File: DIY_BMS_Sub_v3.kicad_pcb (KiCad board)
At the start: 4 copper layers, 70 x 70 mm, 112 parts, among them J1 Conn_01x11, J2 Conn_02x04_Top_Bottom, J3 Conn_02x03_Top_Bottom, J4 Conn_02x03_Top_Bottom, Q1 Q_NMOS_GSD, Q2 Q_NMOS_GSD, Q3 Q_NMOS_GSD, Q4 Q_NMOS_GSD, Q5 Q_NMOS_GSD, Q6 Q_NMOS_GSD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

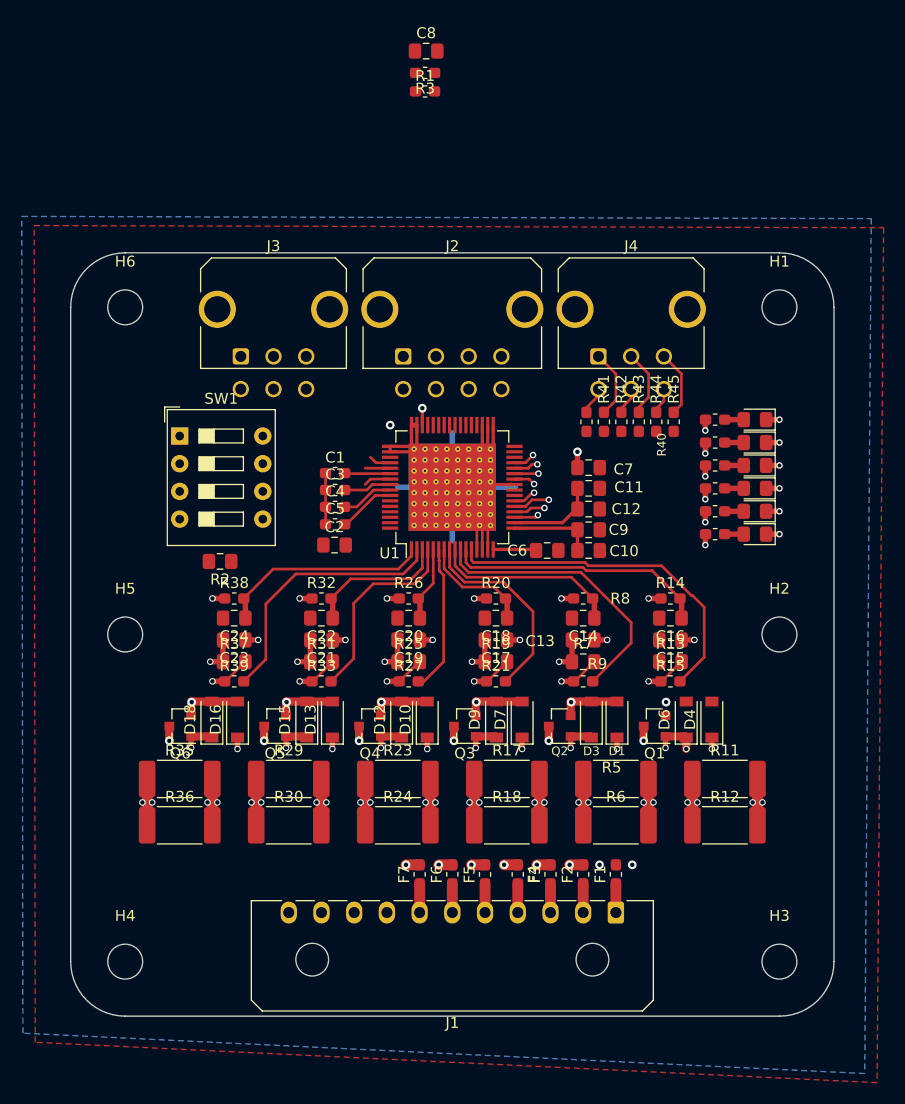
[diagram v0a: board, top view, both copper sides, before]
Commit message: Add files via upload
Routed the PCB further (switch-, NORTH- and thermistor still have to be done). Made silkscreen spacing more consistant overall. Added 3d-files for Molex-connectors.
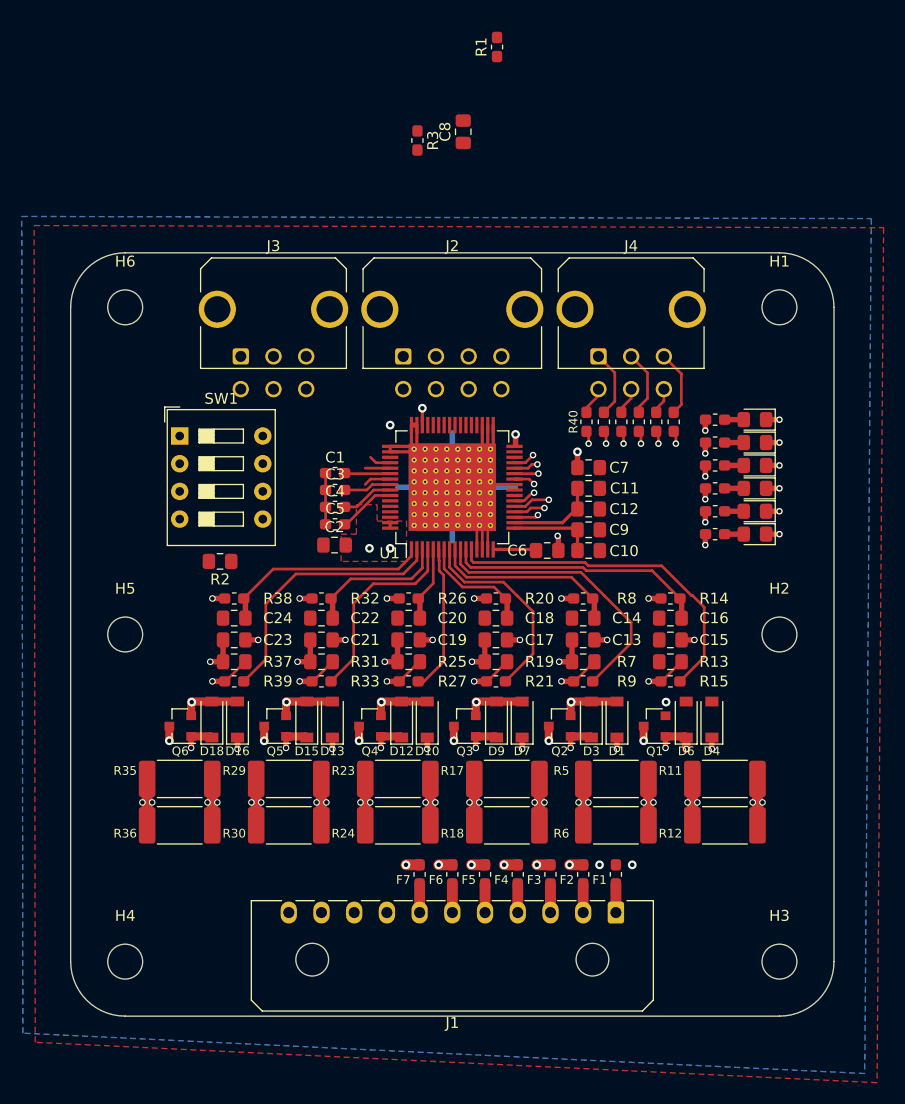
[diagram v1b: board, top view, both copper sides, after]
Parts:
- moved C8 8.14 mm to (1.00, -46.1), turned to 90 degrees
- moved R1 7.76 mm to (4.10, -53.9), turned to 90 degrees
- moved R3 6.24 mm to (-3.20, -45.3), turned to 270 degrees
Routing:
- net /C6: track 30.4 -> 114.8 mm, vias 7 -> 9
- net Net-(D17-Pad1): track 14.0 -> 87.1 mm
- net /C5: track 55.2 -> 120.2 mm
- net Net-(D14-Pad1): track 13.5 -> 76.6 mm
- net /C4: track 45.1 -> 104.4 mm
- net /C3: track 45.2 -> 103.1 mm
- net Net-(D11-Pad1): track 13.4 -> 66.7 mm
- net Net-(D8-Pad1): track 14.0 -> 57.5 mm
- net /C2: track 51.2 -> 94.4 mm
- net Net-(D2-Pad1): track 14.5 -> 49.0 mm
- net /C1: track 59.8 -> 89.3 mm
- net Net-(D5-Pad1): track 19.0 -> 46.7 mm
- net Net-(R45-Pad2): track 2.28 -> 20.0 mm, vias 1 -> 2
- net Net-(R44-Pad2): track 2.24 -> 18.1 mm, vias 1 -> 2
- net Net-(R43-Pad2): track 2.30 -> 16.8 mm, vias 1 -> 2
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- added copper zone on F.Cu, net /C6

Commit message: Add files via upload
Routed external thermistor and HOST-interface traces. Added silkscreen text. Placed additional AGND-via's.
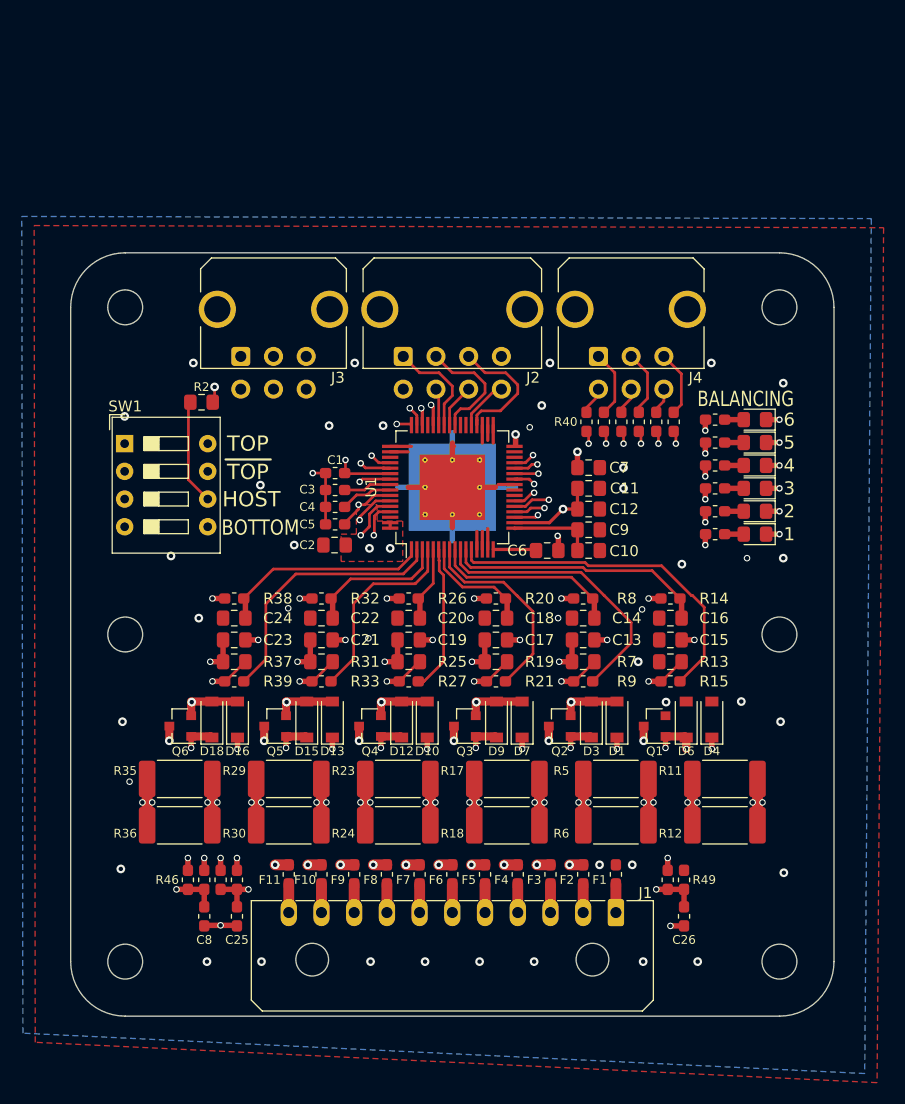
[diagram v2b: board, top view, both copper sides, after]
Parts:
- added C25: 33p, Capacitor_SMD:C_0603_1608Metric_Pad1.05x0.95mm_HandSolder, F.Cu at (-19.8, 25.9)
- added C26: 33p, Capacitor_SMD:C_0603_1608Metric_Pad1.05x0.95mm_HandSolder, F.Cu at (21.2, 25.9)
- added F10: 2A, Fuse:Fuse_0603_1608Metric_Pad1.05x0.95mm_HandSolder, F.Cu at (-12.0, 22.0)
- added F11: 2A, Fuse:Fuse_0603_1608Metric_Pad1.05x0.95mm_HandSolder, F.Cu at (-15.0, 22.0)
- added F8: 2A, Fuse:Fuse_0603_1608Metric_Pad1.05x0.95mm_HandSolder, F.Cu at (-6.00, 22.0)
- added F9: 2A, Fuse:Fuse_0603_1608Metric_Pad1.05x0.95mm_HandSolder, F.Cu at (-9.00, 22.0)
- added R46: 1K82, Resistor_SMD:R_0603_1608Metric_Pad1.05x0.95mm_HandSolder, F.Cu at (-24.2, 22.5)
- added R47: 1K47, Resistor_SMD:R_0603_1608Metric_Pad1.05x0.95mm_HandSolder, F.Cu at (-22.8, 22.5)
- added R48: 1K82, Resistor_SMD:R_0603_1608Metric_Pad1.05x0.95mm_HandSolder, F.Cu at (19.8, 22.5)
- added R49: 1K47, Resistor_SMD:R_0603_1608Metric_Pad1.05x0.95mm_HandSolder, F.Cu at (21.2, 22.5)
- C8: value 47p -> 33p; footprint Capacitor_SMD:C_0805_2012Metric_Pad1.15x1.40mm_HandSolder -> Capacitor_SMD:C_0603_1608Metric_Pad1.05x0.95mm_HandSolder
- U1: footprint Package_QFP:HTQFP-64-1EP_10x10mm_P0.5mm_EP8x8mm_Mask4.4x4.4mm_ThermalVias -> #_custom_footprints:HTQFP-64-1EP_10x10mm_P0.5mm_EP8x8mm_Mask4.4x4.4mm_LessThermalVias
- moved R1 80.5 mm to (-21.2, 22.5), turned to 270 degrees
- moved C8 75.8 mm to (-22.8, 25.9), turned to 270 degrees
- moved R3 69.8 mm to (-19.8, 22.5), turned to 90 degrees
- moved R2 14.7 mm to (-23.0, -21.3)
- moved SW1 5.10 mm to (-30.1, -17.5)
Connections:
- J1 pad 10: (no net) -> Net-(F10-Pad1)
- J1 pad 11: (no net) -> Net-(F11-Pad1)
- J1 pad 8: (no net) -> Net-(F8-Pad1)
- J1 pad 9: (no net) -> Net-(F9-Pad1)
- J2 pad 1: (no net) -> SDI_H
- J2 pad 2: (no net) -> SCLK_H
- J2 pad 3: (no net) -> CONV_H
- J2 pad 4: (no net) -> LDOD
- J2 pad 5: (no net) -> AGND
- J2 pad 6: (no net) -> CS_H
- J2 pad 7: (no net) -> SDO_H
- J2 pad 8: (no net) -> DRDY_H
- R1 pad 2: Net-(C8-Pad1) -> Net-(C25-Pad1)
- R3 pad 1: Net-(C8-Pad1) -> Net-(C25-Pad1)
- R3 pad 2: (no net) -> TS1
- U1 pad 20: Net-(C8-Pad1) -> Net-(C25-Pad1)
- U1 pad 36: (no net) -> CONV_H
- U1 pad 37: (no net) -> DRDY_H
- U1 pad 40: (no net) -> SCLK_H
- U1 pad 41: (no net) -> SDO_H
- U1 pad 42: (no net) -> SDI_H
- U1 pad 43: (no net) -> CS_H
- U1 pad 47: AGND -> Net-(R48-Pad1)
- U1 pad 48: AGND -> Net-(C26-Pad1)
- U1 pad 60: (no net) -> Net-(R46-Pad1)
- U1 pad 61: (no net) -> Net-(C8-Pad1)
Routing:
- net 5VDC: track 2.88 -> 168.5 mm, vias 2 -> 7
- net Net-(R48-Pad1): track 0.00 -> 92.9 mm, vias 0 -> 2
- net Net-(C26-Pad1): track 0.00 -> 89.8 mm, vias 0 -> 3
- net Net-(C25-Pad1): track 0.00 -> 74.8 mm, vias 0 -> 3
- net Net-(R1-Pad1): track 2.23 -> 64.5 mm, vias 1 -> 2
- net Net-(C8-Pad1): track 2.89 -> 63.2 mm, vias 1 -> 2
- net Net-(R46-Pad1): track 0.00 -> 51.6 mm, vias 0 -> 2
- net SW_Host: track 0.00 -> 48.3 mm, vias 0 -> 1
- net CONV_S: track 2.58 -> 43.7 mm
- net LDOD: track 9.87 -> 40.6 mm, vias 1 -> 3
- net CONV_N: track 0.00 -> 27.7 mm, vias 0 -> 1
- net AGND: track 84.4 -> 63.3 mm, vias 5 -> 40
- net DRDY_N: track 5.27 -> 23.7 mm, vias 0 -> 1
- net /C6: track 114.8 -> 132.4 mm
- net SDO_N: track 4.27 -> 17.7 mm, vias 0 -> 1
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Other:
- board text added: "1"
- board text added: "2"
- board text added: "3"
- board text added: "4"
- board text added: "5"
- board text added: "6"
- board text added: "BALANCING"
- board text added: "BOTTOM"
- board text added: "HOST"
- board text added: "TOP"

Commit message: Add files via upload
Added and routed board NTC. Added connector and board info silkscreen. Made keep-out zones for AGND to remove planes under components.
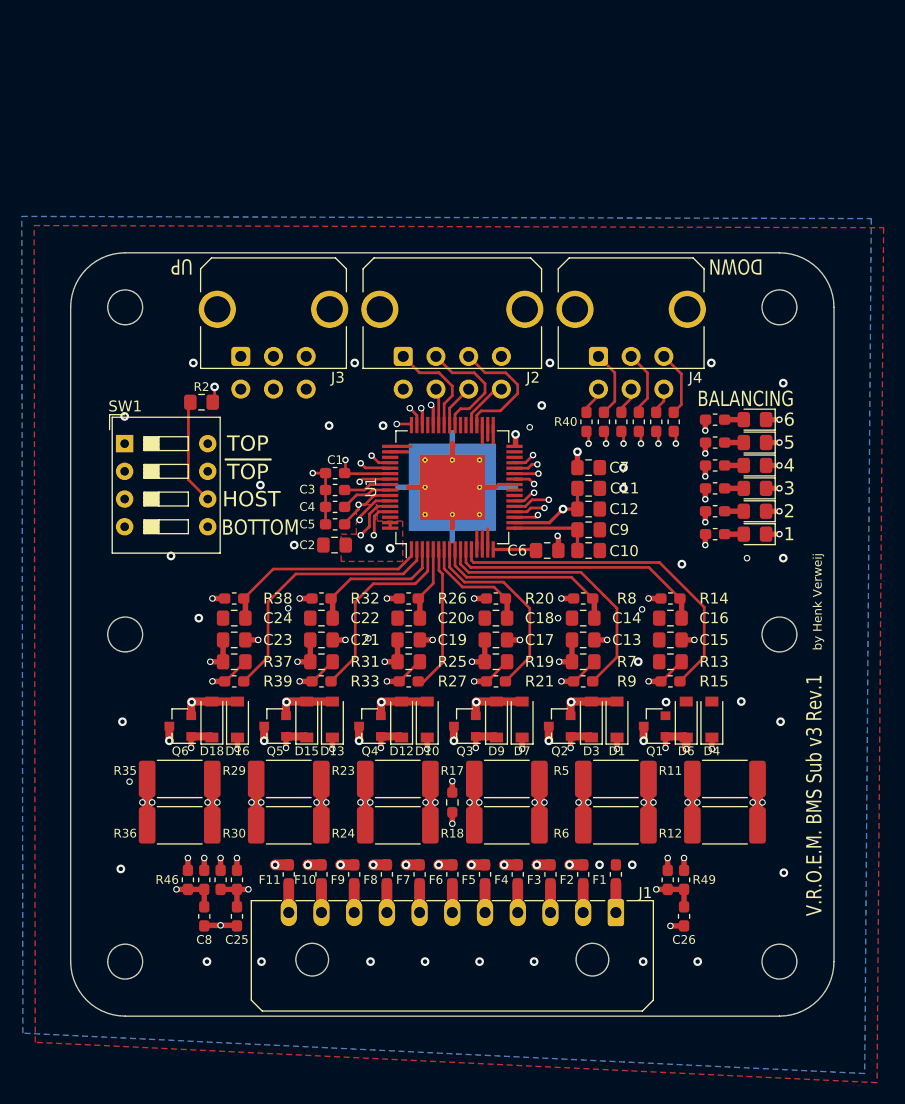
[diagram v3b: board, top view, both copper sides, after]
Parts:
- added TH1: 10K NTC, Resistor_SMD:R_0603_1608Metric_Pad0.98x0.95mm_HandSolder, F.Cu at (0.00, 15.4)
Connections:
- R49 pad 2: (no net) -> Net-(R49-Pad2)
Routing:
- net Net-(R49-Pad2): track 0.00 -> 25.4 mm, vias 0 -> 2
- net 5VDC: track 168.5 -> 181.3 mm, vias 7 -> 8
- net Net-(C26-Pad1): track 89.8 -> 91.4 mm
- net /S2_components/Balancing: track 26.3 -> 25.2 mm
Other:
- board text added: "DOWN"
- board text added: "S0"
- board text added: "S1"
- board text added: "S2"
- board text added: "S3"
- board text added: "S4"
- board text added: "S5"
- board text added: "S6"
- board text added: "T1+"
- board text added: "T1-"
- board text added: "T2+"
- board text added: "T2-"
- board text added: "UP"
- board text added: "V.R.O.E.M. BMS Sub v3 Rev.1"
- board text added: "V.R.O.E.M. BMS Sub v3 Rev.1 by Henk Verweij"
- board text added: "by Henk Verweij"

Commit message: Add files via upload
Placed additional via's to BQ76-IC and removed soldermask beneath (to allow for soldering of thermal pad without hot air). Generated GERBER-, BOM- (for SMD parts) and POS-file.
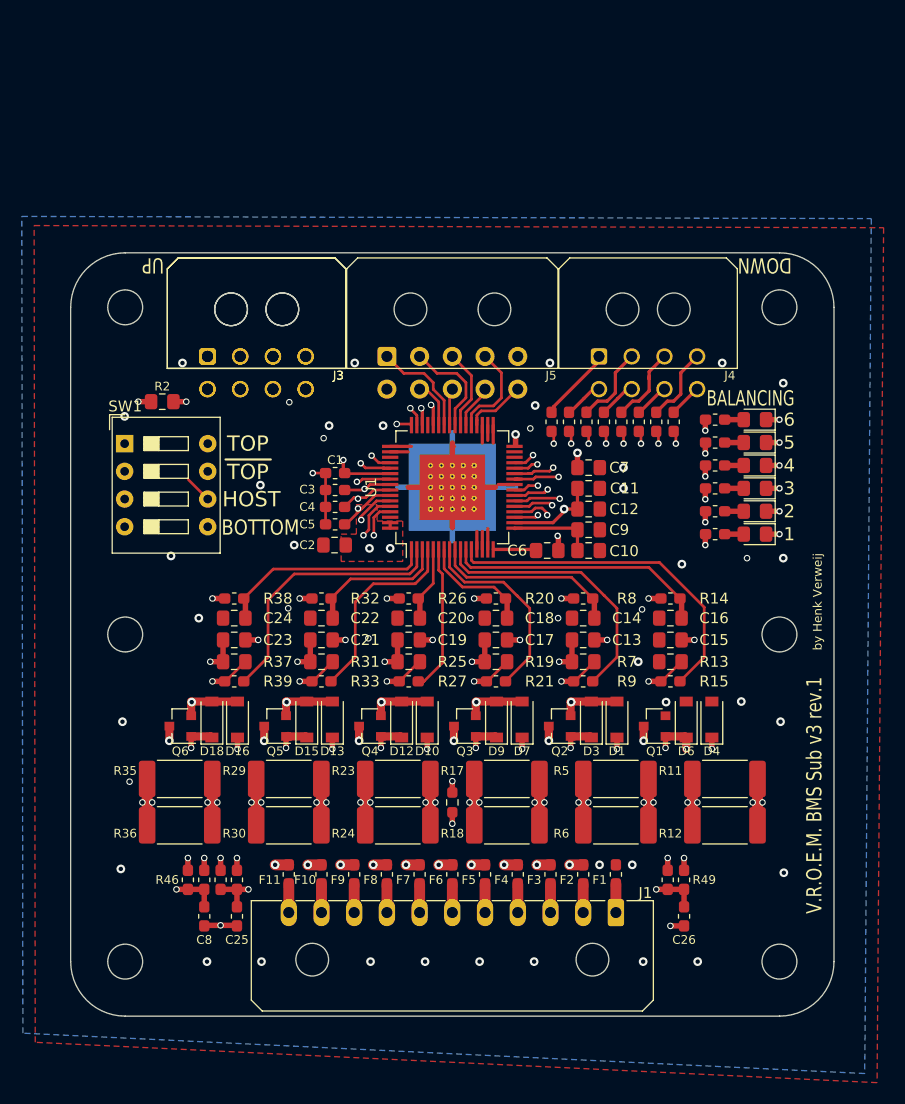
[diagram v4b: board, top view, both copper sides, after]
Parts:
- removed J2: Conn_02x04_Top_Bottom, Connector_Molex:Molex_Micro-Fit_3.0_43045-0821_2x04-1MP_P3.00mm_Horizontal
- removed the J3 at (-19.4, -25.5)
- added J3 (x2): Conn_02x04_Top_Bottom, Connector_Molex:Molex_Micro-Fit_3.0_43045-0800_2x04_P3.00mm_Horizontal, F.Cu at (-22.4, -25.5)
- added J5: Conn_02x05_Top_Bottom, Connector_Molex:Molex_Micro-Fit_3.0_43045-1000_2x05_P3.00mm_Horizontal, F.Cu at (-6.00, -25.5)
- added R50: 1k, Resistor_SMD:R_0603_1608Metric_Pad1.05x0.95mm_HandSolder, F.Cu at (10.7, -19.5)
- added R51: 1k, Resistor_SMD:R_0603_1608Metric_Pad1.05x0.95mm_HandSolder, F.Cu at (9.10, -19.5)
- J4: value Conn_02x03_Top_Bottom -> Conn_02x04_Top_Bottom; footprint Connector_Molex:Molex_Micro-Fit_3.0_43045-0621_2x03-1MP_P3.00mm_Horizontal -> Connector_Molex:Molex_Micro-Fit_3.0_43045-0800_2x04_P3.00mm_Horizontal
- moved R2 3.60 mm to (-26.6, -21.4)
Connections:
- J4 pad 1: DRDY_S -> CS_S
- J4 pad 3: CS_S -> FAULT_S
- J4 pad 4: CONV_S -> DRDY_S
- J4 pad 5: SCLK_S -> SDI_S
- J4 pad 6: SDI_S -> SCLK_S
- R40 pad 1: CONV_S -> SDO_S
- R41 pad 1: DRDY_S -> SCLK_S
- R42 pad 1: SCLK_S -> FAULT_S
- R43 pad 1: SDO_S -> ALERT_S
- R44 pad 1: SDI_S -> DRDY_S
- R45 pad 1: CS_S -> CONV_S
- U1 pad 21: Net-(R40-Pad2) -> Net-(R45-Pad2)
- U1 pad 22: Net-(R41-Pad2) -> Net-(R44-Pad2)
- U1 pad 23: (no net) -> Net-(R43-Pad2)
- U1 pad 24: (no net) -> Net-(R42-Pad2)
- U1 pad 26: Net-(R42-Pad2) -> Net-(R41-Pad2)
- U1 pad 27: Net-(R43-Pad2) -> Net-(R40-Pad2)
- U1 pad 28: Net-(R44-Pad2) -> Net-(R50-Pad2)
- U1 pad 29: Net-(R45-Pad2) -> Net-(R51-Pad2)
- U1 pad 38: (no net) -> ALERT_H
- U1 pad 39: (no net) -> FAULT_H
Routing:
- net 5VDC: track 181.3 -> 210.3 mm
- net ALERT_N: track 5.24 -> 25.2 mm, vias 0 -> 1
- net FAULT_N: track 4.38 -> 24.0 mm, vias 0 -> 2
- net LDOD: track 40.6 -> 21.3 mm
- net CONV_N: track 27.7 -> 46.7 mm, vias 1 -> 2
- net SCLK_N: track 15.1 -> 27.4 mm
- net CONV_S: track 43.7 -> 55.0 mm
- net CS_N: track 13.6 -> 22.7 mm
- net SDI_N: track 12.3 -> 21.0 mm
- net FAULT_S: track 0.00 -> 7.72 mm
- net FAULT_H: track 0.00 -> 7.41 mm
- net Net-(R50-Pad2): track 0.00 -> 7.34 mm, vias 0 -> 2
- net CONV_H: track 12.3 -> 6.51 mm
- net Net-(R51-Pad2): track 0.00 -> 5.74 mm, vias 0 -> 2
- net ALERT_H: track 0.00 -> 4.87 mm
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- added copper zone on In1.Cu, net LDOD
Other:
- board text added: "V.R.O.E.M. BMS Sub v3 rev.1"
- board text added: "V.R.O.E.M. BMS Sub v3 rev.1 by Henk Verweij"
- board text removed: "V.R.O.E.M. BMS Sub v3 Rev.1"
- board text removed: "V.R.O.E.M. BMS Sub v3 Rev.1 by Henk Verweij"
